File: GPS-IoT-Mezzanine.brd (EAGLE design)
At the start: 60 x 30 mm, 20 parts, among them J1 F-1X02-SIP-100-40, Q1 DTC143ZEBTL, Q2 DTC143ZEBTL, U1 LD1117D33TR, U2 TXS0104ED

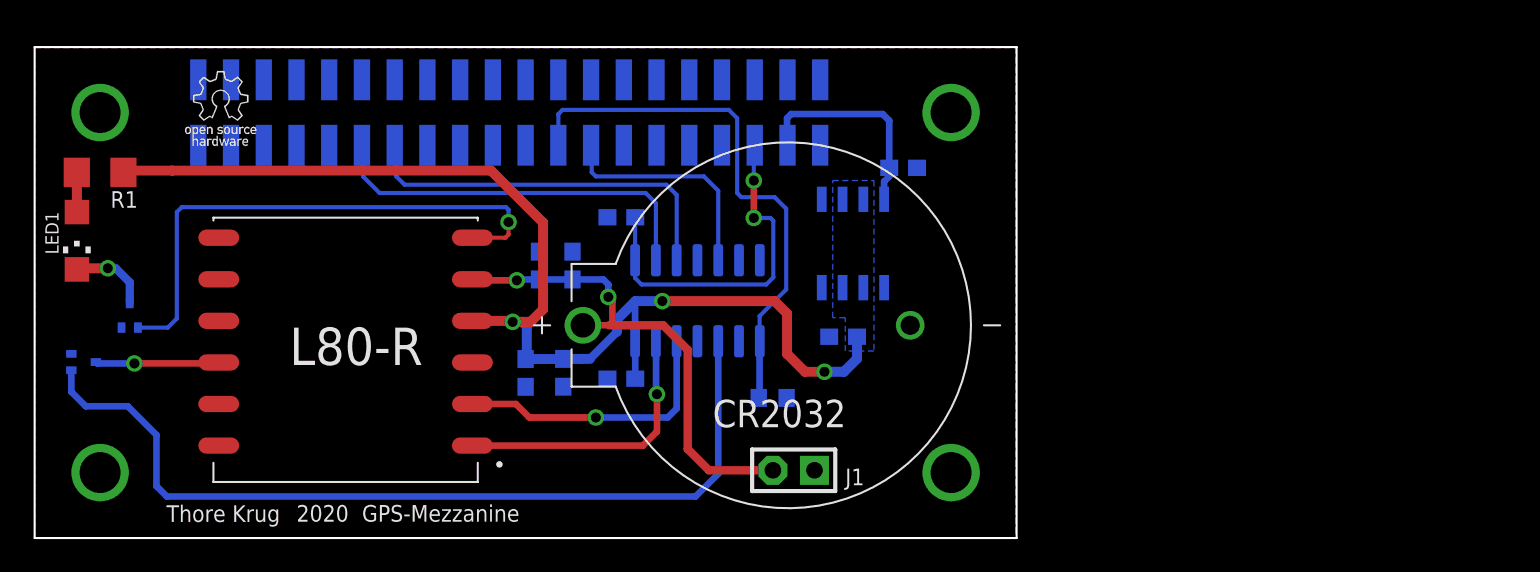
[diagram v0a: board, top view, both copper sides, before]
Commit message: Improvements to the mezzanine
added keepout for the antenna, improved silkscreen on top layer, improved poer traces to the Level shifter IC.

Signed off by Thore Krug opensource[at]thorekrug.de
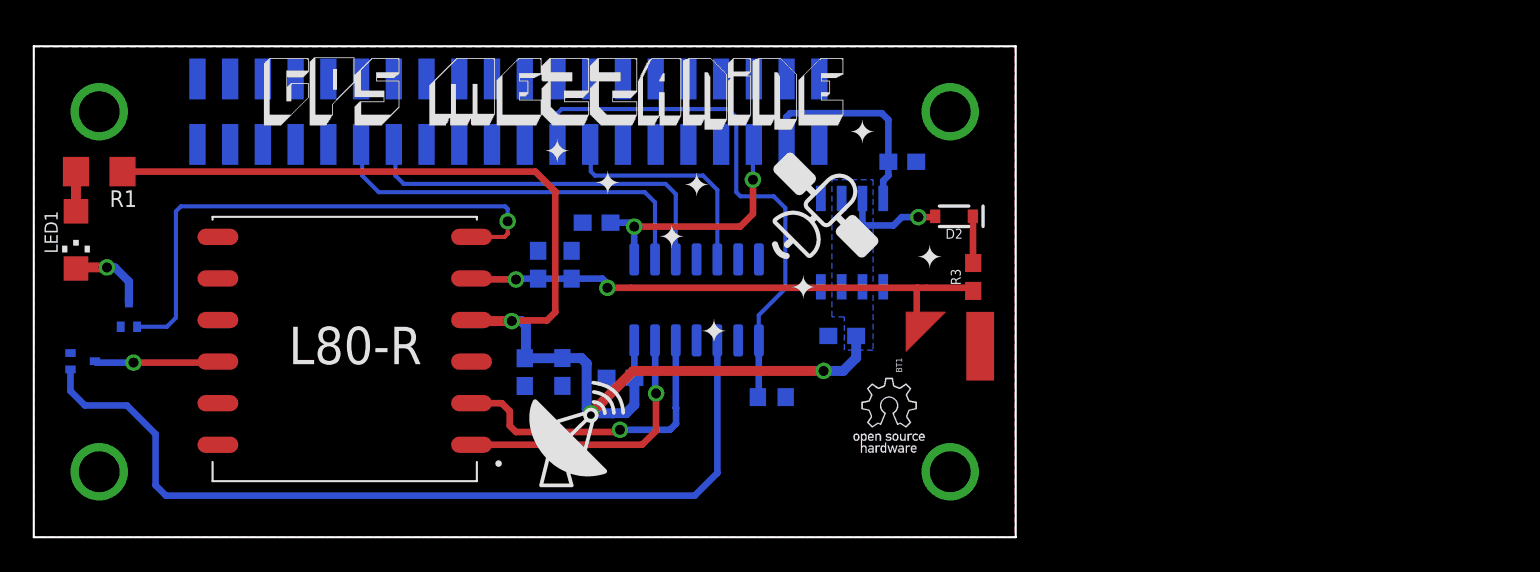
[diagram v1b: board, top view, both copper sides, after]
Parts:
- removed CR2032: BS-7, BS-7:BAT_BS-7
- removed J1: F-1X02-SIP-100-40, con-headers-jp:SIP-100-02-40
- added BT1: 6.8MM_COIN_CELL, SparkFun-Batteries:ML414H_IV01E
- added D2: 0.5A/40V/420mV, SparkFun-DiscreteSemi:SOD-323
- added R3: 3.3k, SparkFun-Resistors:0603
- C8: value 4,7uF -> 1uF
- moved C3 1.55 mm to (34.4, 19.3)
- moved C1 0.37 mm to (53.1, 23.0)
- moved U1 0.07 mm to (50.0, 18.1)
- moved U2 0.07 mm to (40.5, 14.6)
- moved C7 0.07 mm to (30.8, 16.7)
- moved LED1 0.07 mm to (2.58, 18.2)
- moved C8 0.07 mm to (32.9, 16.7)
- moved Q1 0.07 mm to (5.81, 13.7)
- moved Q2 0.07 mm to (2.99, 10.8)
- moved R1 0.07 mm to (4.00, 22.4)
- moved PCB1 0.07 mm to (-0.00, 0.05)
- moved C6 0.07 mm to (30.0, 10.1)
- moved R2 0.07 mm to (45.1, 8.61)
- moved C2 0.07 mm to (49.4, 12.4)
- moved C4 0.07 mm to (35.8, 9.79)
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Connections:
- new net N$6: D2.C, R3.2
- net +3V3: now also D2.A
- net GND: now also BT1.-; no longer CR2032.-, J1.1
- net V_BCKP: now also BT1.+, R3.1; no longer CR2032.+, J1.2
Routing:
- net +3V3: track 71.9 -> 82.0 mm, vias 3 -> 4
- net +1V8: track 21.7 -> 15.4 mm
- net V_BCKP: track 30.0 -> 33.3 mm
- net N$6: track 0.00 -> 2.87 mm
- net L80-TX: track 17.2 -> 19.1 mm
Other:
- board text removed: "2020"
- board text removed: "GPS-Mezzanine"
- board text removed: "Thore Krug"

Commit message: Board Update + BOM
Added Round Corner to make the Board more pleasing to the eye, added current limiting resistor for the pink status LED indication 1PPS ( 1 Puls per Second ) created by the L80-R GPS Module. Added BOM ( Bill of material ) in CSV format in the folder misc. Added Missing Datasheets.

Signed off by: Thore Krug opensource[at]thorekrug.de
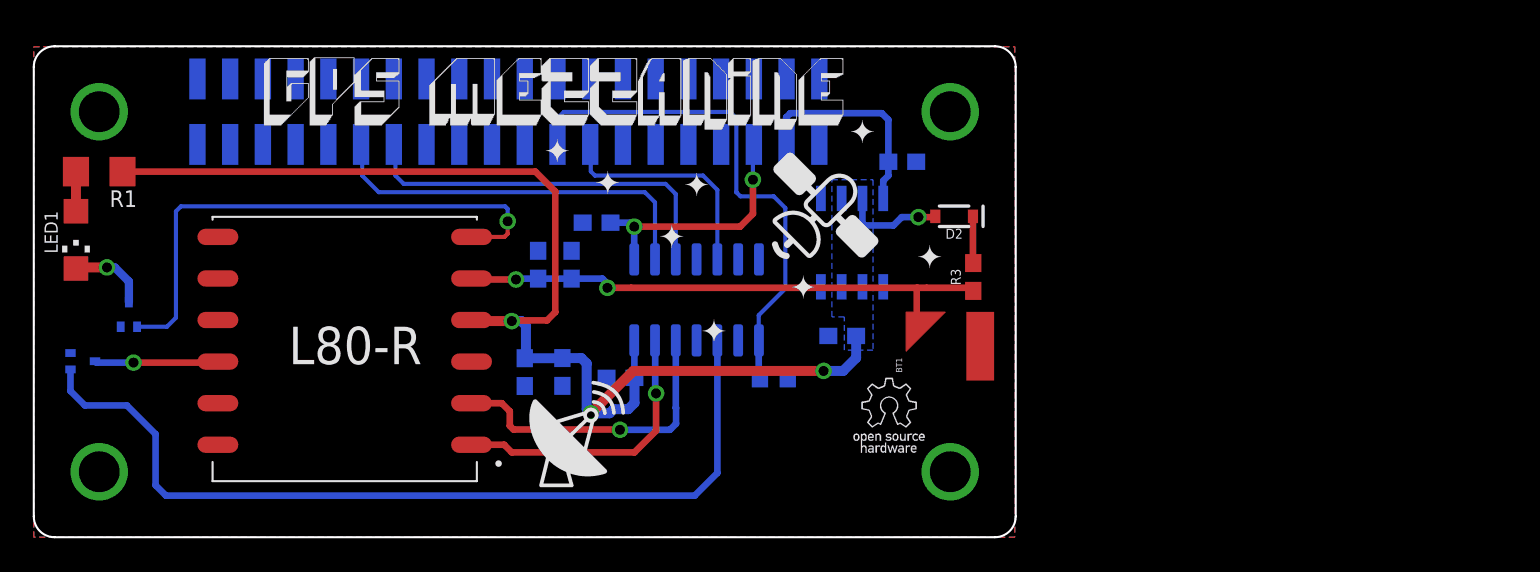
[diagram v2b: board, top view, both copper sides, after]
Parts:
- LED1: value (none) -> OSK51206C1E ( Pink )
- PCB1: value 96BOARDS-IOT-1.8V -> 96BOARDS-IOT-MEZZANINE_96BOARDS-IOT-1.8V; device 96Boards-IoT-Mezzanine:96BOARDS-IOT-1.8V -> GPS-IoT-Mezzanine:96BOARDS-IOT-MEZZANINE_96BOARDS-IOT-1.8V
- R1: value (none) -> 10R
- moved R2 1.15 mm to (45.2, 9.76)
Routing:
- net GPIO-A: track 33.4 -> 31.9 mm
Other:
- outline, holes or cut-outs redrawn

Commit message: Updated PCB
Update of PCB ( Disable thermal relief for the mounting holes )

Signed off by: Thore Krug opensource[at]thorekrug.de
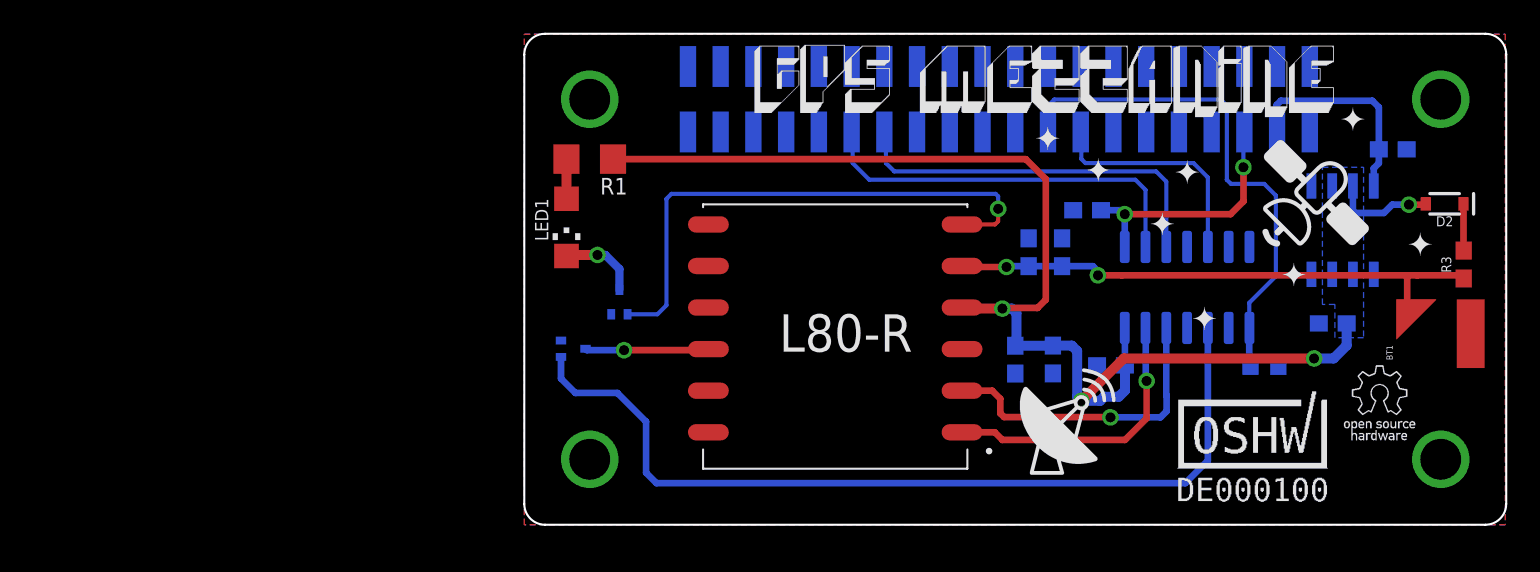
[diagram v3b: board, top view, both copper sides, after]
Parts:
- moved C4 30.0 mm to (65.8, 10.5)
- moved BT1 30.0 mm to (86.0, 11.9)
- moved C2 30.0 mm to (79.4, 13.1)
- moved C5 30.0 mm to (62.3, 10.9)
- moved C7 30.0 mm to (60.8, 17.5)
- moved C8 30.0 mm to (62.8, 17.5)
- moved D2 30.0 mm to (86.2, 20.4)
- moved PCB1 30.0 mm to (30.0, 0.81)
- moved Q1 30.0 mm to (35.8, 14.4)
- moved Q2 30.0 mm to (33.0, 11.6)
- moved R1 30.0 mm to (34.0, 23.2)
- moved U1 30.0 mm to (80.0, 18.8)
- moved U2 30.0 mm to (70.5, 15.3)
- moved C6 30.0 mm to (60.0, 10.9)
- moved L80-R 30.0 mm to (49.0, 12.8)
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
